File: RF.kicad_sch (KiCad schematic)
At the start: 31 parts, among them J4 SMA, J5 SMA, J6 U.FL-R-SMT-1(80), U4 RFX2401C, U5 2450BM14A0002T, U6 2450BP39D100CE, U7 nRF24L01P, U8 E220-400M30S, U9 MAX-M10S, Y1 ECS-160-9-33B-CTP-TR

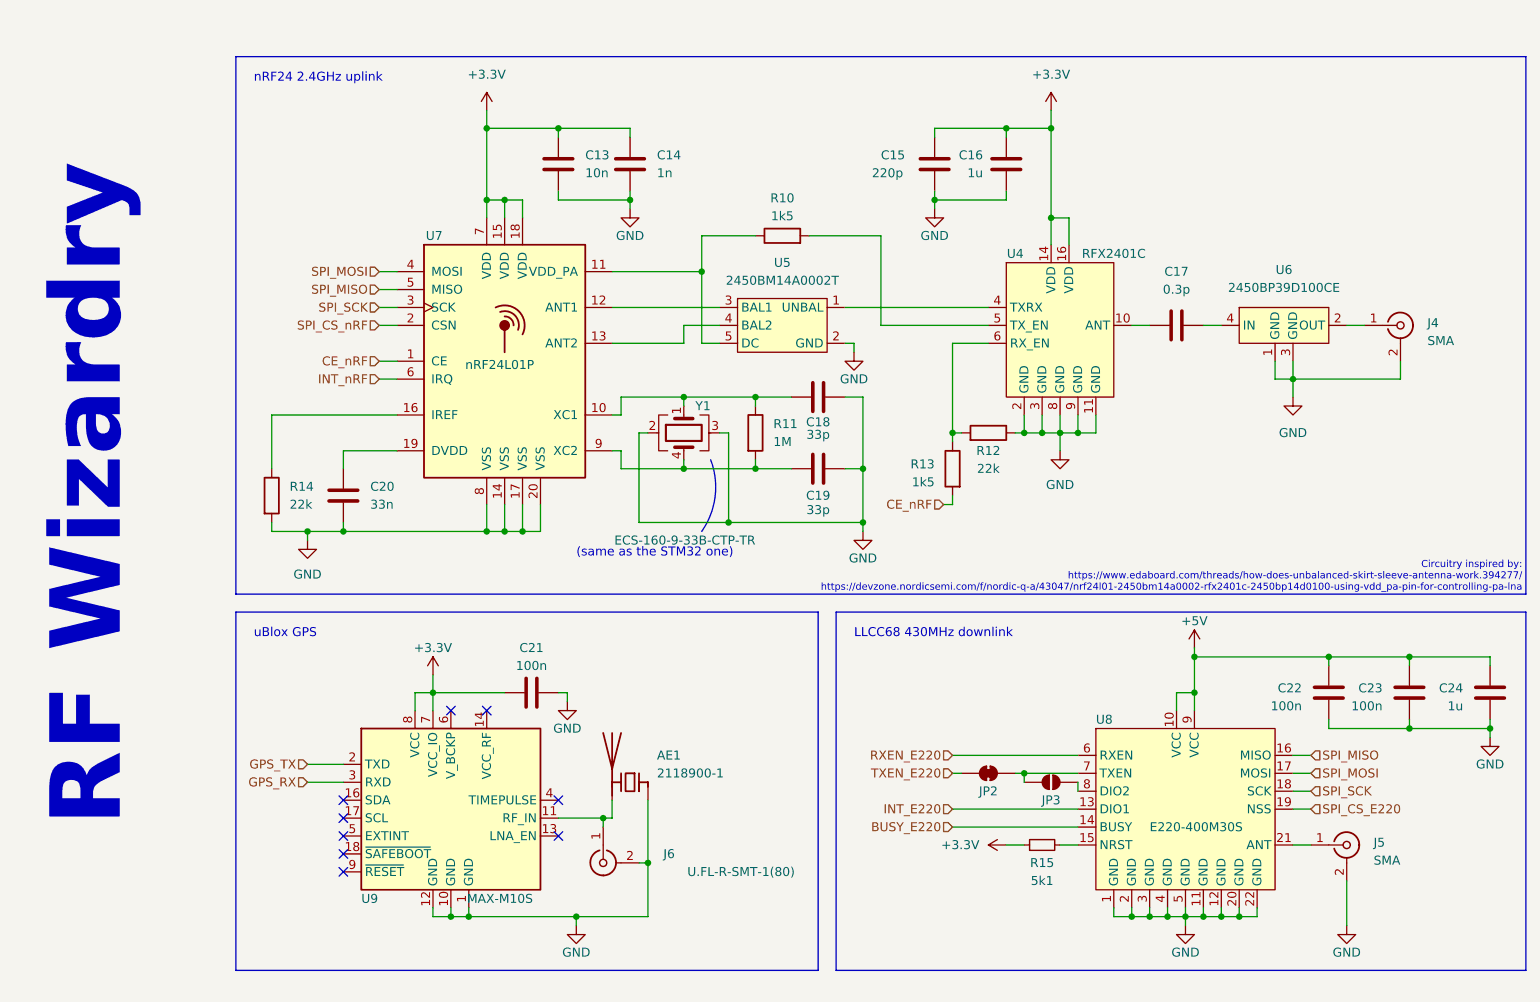
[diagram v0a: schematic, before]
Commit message: :children_crossing: Add test pads and assign footprints
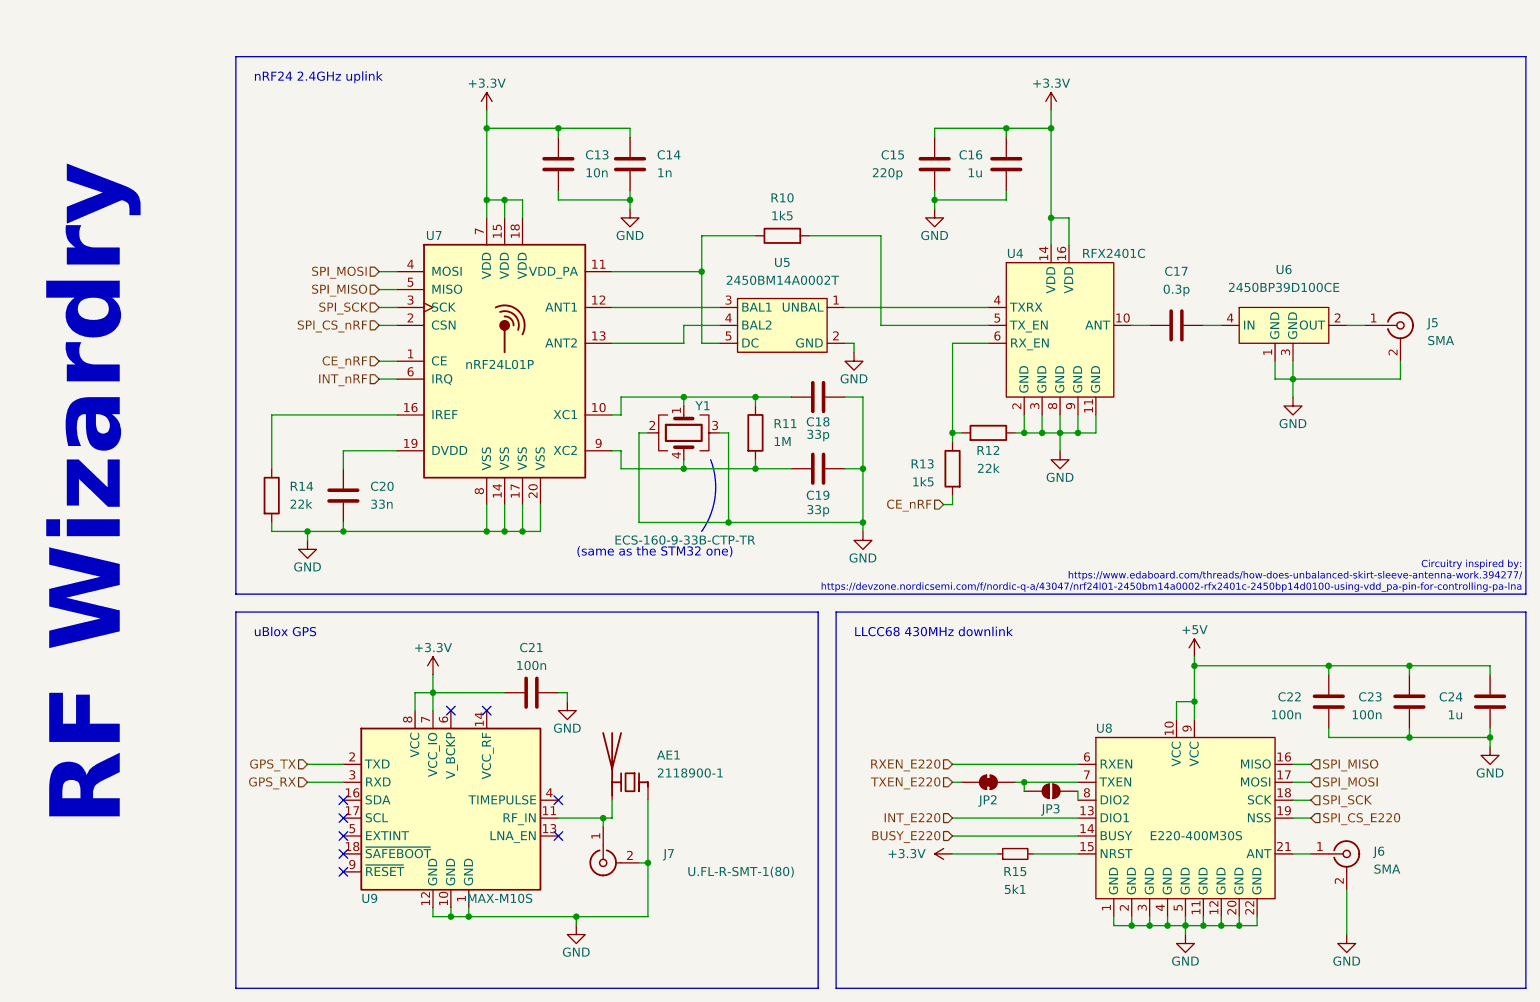
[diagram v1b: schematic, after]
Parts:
- renumbered J4 to J5, J5 to J6, J6 to J7
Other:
- moved on the sheet: C22, C23, C24, J6, JP2, JP3, R15, U8
